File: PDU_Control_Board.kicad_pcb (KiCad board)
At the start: 4 copper layers, 237.7 x 87.4 mm, 269 parts

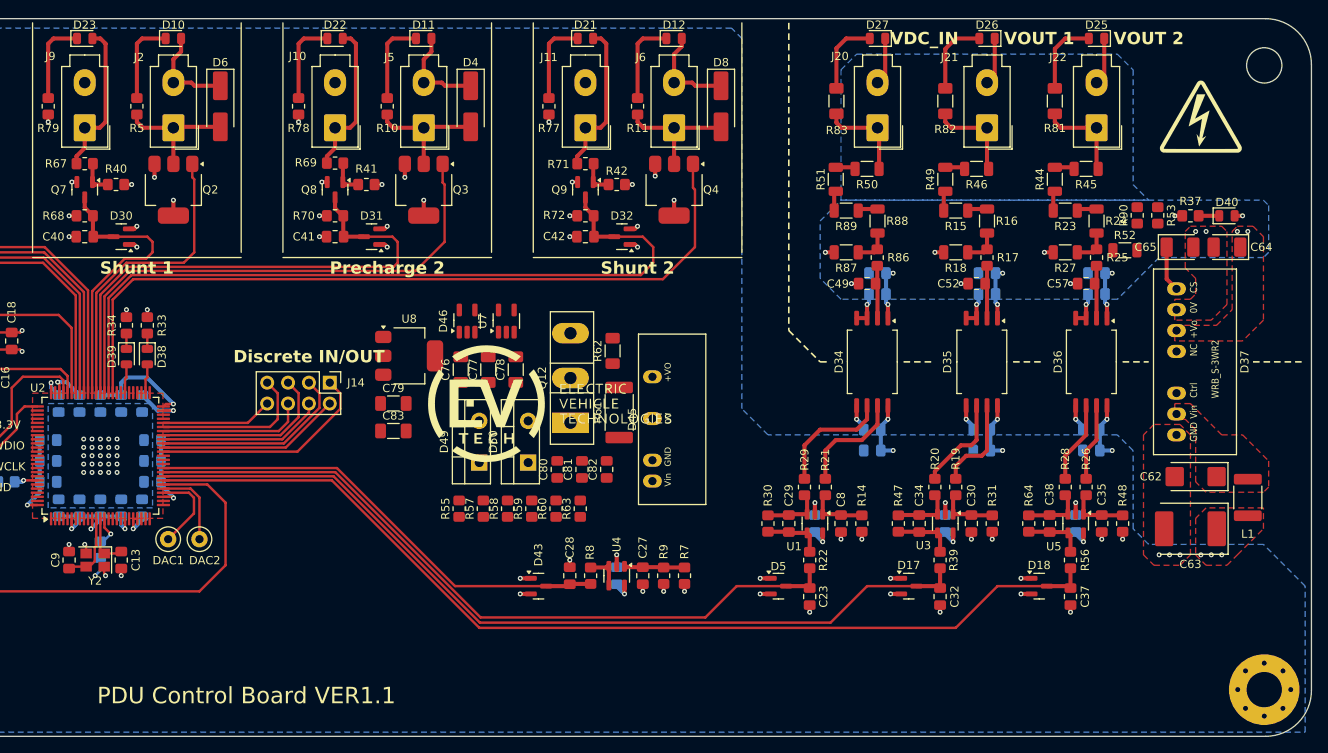
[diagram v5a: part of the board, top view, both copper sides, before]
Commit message: VER1.2: добавил защиту по высокому
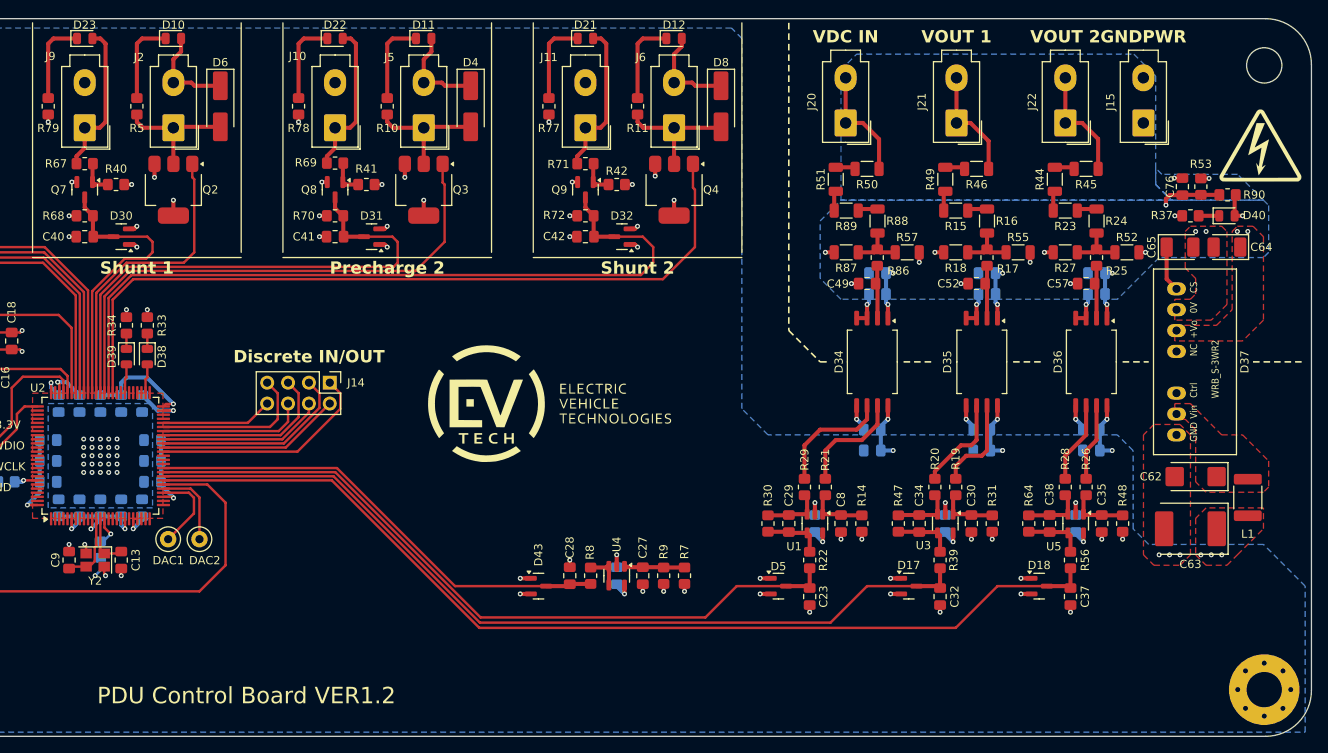
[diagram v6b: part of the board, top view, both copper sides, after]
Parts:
- removed C77: 4.7u, Capacitor_SMD:C_1206_3216Metric_Pad1.33x1.80mm_HandSolder
- removed C78, C79, C83: 10u, Capacitor_SMD:C_1206_3216Metric_Pad1.33x1.80mm_HandSolder
- removed C80: 100n, Capacitor_SMD:C_0805_2012Metric_Pad1.18x1.45mm_HandSolder
- removed C81, C82: 5.6n, Capacitor_SMD:C_0805_2012Metric_Pad1.18x1.45mm_HandSolder
- removed D25, D26, D27: ~, LED_SMD:LED_0805_2012Metric
- removed D45: ~, MORNSUN:B_S-2WR3
- removed D46, U7: ~, Package_TO_SOT_SMD:SOT-23-5_HandSoldering
- removed D49, D50: ~, Package_TO_SOT_THT:TO-220-2_Vertical
- removed Q12: ~, Package_TO_SOT_THT:TO-247-3_Vertical
- removed R58: 200k, Resistor_SMD:R_0805_2012Metric_Pad1.20x1.40mm_HandSolder
- removed R59: 2.37k, Resistor_SMD:R_0805_2012Metric_Pad1.20x1.40mm_HandSolder
- removed R60, R63: 10k, Resistor_SMD:R_0805_2012Metric_Pad1.20x1.40mm_HandSolder
- removed R61: 0.1, Resistor_SMD:R_2512_6332Metric_Pad1.40x3.35mm_HandSolder
- removed R62: 0, Resistor_SMD:R_1206_3216Metric_Pad1.30x1.75mm_HandSolder
- removed R81, R82, R83: 100k, Resistor_SMD:R_1206_3216Metric_Pad1.30x1.75mm_HandSolder
- removed U8: ~, Package_TO_SOT_SMD:SOT-223-3_TabPin2
- added J15: ~, Connector_My:Mini-Fit_01x02_Vertical, F.Cu at (437.5, 174.8)
- C76: value 4.7u -> 100n; footprint Capacitor_SMD:C_1206_3216Metric_Pad1.33x1.80mm_HandSolder -> Capacitor_SMD:C_0805_2012Metric_Pad1.18x1.45mm_HandSolder
- R10, R11, R12, R13, R4, R5, R76, R77, R78, R79, R80: value 5.1k -> 8.2k
- R15, R16, R46, R49, R50, R51, R88, R89: value 23.7k -> 200k
- R18, R87: value 210 -> 1.6k
- R27, R52: value 1k -> 1.6k
- R55: value 200 -> 1.6k; footprint Resistor_SMD:R_0805_2012Metric_Pad1.20x1.40mm_HandSolder -> Resistor_SMD:R_1206_3216Metric
- R57: value 13.3k -> 1.6k; footprint Resistor_SMD:R_0805_2012Metric_Pad1.20x1.40mm_HandSolder -> Resistor_SMD:R_1206_3216Metric
- moved C76 90.6 mm to (442.2, 182.5), turned to -90 degrees
- moved R55 74.9 mm to (422.2, 190.5), turned to 0 degrees
- moved R57 60.3 mm to (408.8, 190.5), turned to 0 degrees
- moved R90 11.3 mm to (447.8, 183.5), turned to 180 degrees
- moved G*** 8.05 mm to (451.8, 177.5) (x2)
- moved R53 6.31 mm to (444.5, 182.5), turned to 90 degrees
- moved J20 3.92 mm to (401.2, 174.8)
- moved J22 3.84 mm to (428.0, 174.8)
- moved J21 3.76 mm to (414.8, 174.8)
- moved R52 0.35 mm to (435.5, 190.5)
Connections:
- C76 pad 1: Net-(D45-Vin) -> GNDPWR
- C76 pad 2: GND -> +1V0
- J20 pad 1: VDC_IN -> VDC
- J20 pad 2: GNDPWR -> VDC
- J21 pad 2: GNDPWR -> VDC_OUT1
- J22 pad 2: GNDPWR -> VDC_OUT2
- R55 pad 1: Net-(D48-K) -> Net-(R16-Pad1)
- R55 pad 2: Net-(D46-IN+) -> +1V0
- R57 pad 1: Net-(D48-K) -> Net-(R57-Pad1)
- R57 pad 2: Net-(U7-+) -> +1V0
- R86 pad 2: Net-(R86-Pad2) -> Net-(R57-Pad1)
- R87 pad 2: Net-(R86-Pad2) -> Net-(R57-Pad1)
- R88 pad 1: Net-(R86-Pad2) -> Net-(R57-Pad1)
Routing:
- net GNDPWR: track 36.9 -> 21.6 mm, vias 12 -> 14
- net VDC: track 0.00 -> 14.0 mm
- net VDC_IN: track 11.4 -> 0.00 mm
- net +1V0: track 0.00 -> 10.7 mm, vias 0 -> 4
- net Net-(D26-A): track 9.47 -> 0.00 mm
- net Net-(D25-A): track 9.47 -> 0.00 mm
- net Net-(D27-A): track 9.44 -> 0.00 mm
- net Net-(R57-Pad1): track 0.00 -> 6.80 mm
- net Net-(R86-Pad2): track 4.46 -> 0.00 mm
- net VDC_OUT2: track 11.4 -> 14.2 mm
- net +3.3VP: track 20.3 -> 22.9 mm
- net VDC_OUT1: track 11.4 -> 14.0 mm
- net Net-(R16-Pad1): track 4.48 -> 6.95 mm
- net Net-(R24-Pad1): track 4.48 -> 6.87 mm
- added copper zone on In1.Cu, net +1V0
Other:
- board text added: "GNDPWR"
- board text added: "PDU Control Board VER1.2"
- board text added: "VDC IN"
- board text removed: "PDU Control Board VER1.1"
- board text removed: "VDC_IN"
